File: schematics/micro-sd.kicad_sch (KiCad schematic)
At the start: 3 parts, among them J3 PJS008-4100-0-VE

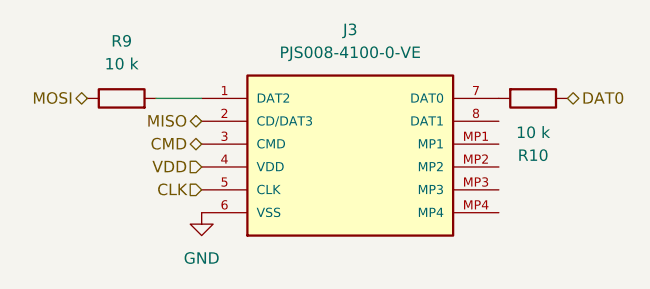
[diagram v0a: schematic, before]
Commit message: Integrated 3V3 buck converter due to Arduino's current limits
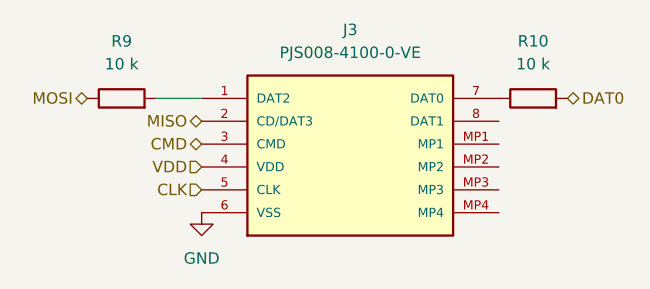
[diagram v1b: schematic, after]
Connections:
- net DAT0: now also R10.2; no longer R10.1
- net at J3.7 (DAT0): now also R10.1; no longer R10.2
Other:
- moved on the sheet: R10
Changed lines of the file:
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@@
 	(symbol
 		(lib_id "Device:R")
-		(at 161.29 85.09 270)
+		(at 161.29 85.09 90)
 		(unit 1)
 		(exclude_from_sim no)
@@
 		(fields_autoplaced yes)
 		(property "Reference" "R10"
-			(at 161.29 91.44 90)
+			(at 161.29 78.74 90)
 			(effects
 				(font
@@
 		)
 		(property "Value" "10 k"
-			(at 161.29 88.9 90)
+			(at 161.29 81.28 90)
 			(effects
 				(font
@@
 		)
 		(property "Footprint" "Resistor_SMD:R_0603_1608Metric"
-			(at 161.29 83.312 90)
+			(at 161.29 86.868 90)
 			(effects
 				(font

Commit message: Fix micro sd connector wiring
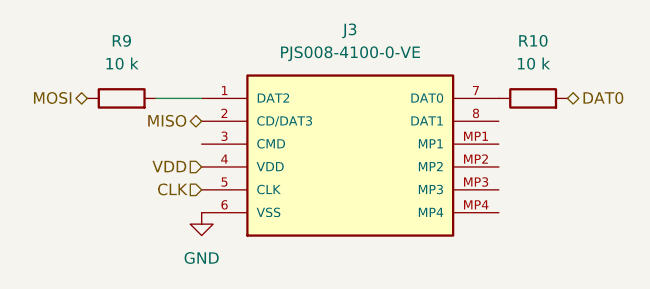
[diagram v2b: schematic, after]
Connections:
- net CMD: no longer names the net of J3.3 (CMD)
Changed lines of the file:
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@@
-		)
-	)
-	(hierarchical_label "CMD"
-		(shape bidirectional)
-		(at 124.46 90.17 180)
-		(effects
-			(font
-				(size 1.27 1.27)
-			)
-			(justify right)
 		)
 	)
